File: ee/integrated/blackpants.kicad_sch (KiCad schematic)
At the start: 24 parts, among them J3 Conn_ARM_SWD_TagConnect_TC203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, SW1 SW_Push, U1 STM32F042C6Ux, U11 TPSGM7227YUWQ10G

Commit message: Added a523 components.
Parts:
- removed C10, C11, C33, C6, C8, C9: 100nF, Capacitor_SMD:C_0402_1005Metric, symbol Device:C_Small
- removed C7: 1uF, Capacitor_SMD:C_0402_1005Metric, symbol Device:C_Small
- removed D6: LED, LED_SMD:LED_0603_1608Metric, symbol Device:LED
- removed J3: Conn_ARM_SWD_TagConnect_TC2030-NL, Connector:Tag-Connect_TC2030-IDC-NL_2x03_P1.27mm_Vertical, symbol Connector:Conn_ARM_SWD_TagConnect_TC2030-NL
- removed R2, R33: 1k, Resistor_SMD:R_0402_1005Metric, symbol Device:R
- removed R26: 100K, Resistor_SMD:R_0402_1005Metric, symbol Device:R_Small
- removed SW1: SW_Push, Button_Switch_SMD:SW_Push_1P1T_NO_CK_KSC7xxJ, symbol Switch:SW_Push
- removed TP2, TP3: TestPoint, TestPoint:TestPoint_Pad_1.0x1.0mm, symbol Connector:TestPoint
- removed U1: STM32F042C6Ux, Package_DFN_QFN:QFN-48-1EP_7x7mm_P0.5mm_EP5.6x5.6mm, symbol MCU_ST_STM32F0:STM32F042C6Ux
- removed U11: TPSGM7227YUWQ10G, Package_DFN_QFN:UQFN-10_1.4x1.8mm_P0.4mm, symbol Interface_USB:FSUSB42MUX
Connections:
- no-connect marks 0 -> 1
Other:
- sheet USB renamed USB Hub
- removed sheet DSI Bridge and Backlight
- removed sheet Hardware
- removed sheet Keyboard
- added sheet 2GB LPDDR4 (a523_memory.kicad_sch)
- added sheet 5V / 3.3V peripherals (peripheral_power.kicad_sch)
- added sheet A523 SD and GPIO (a523_gpio.kicad_sch)
- added sheet A523 Standby IO (a523_always_on_io.kicad_sch)
- added sheet A523 USB PHY (a523_usb.kicad_sch)
- added sheet AXP717C + AXP323 (a523_power.kicad_sch)
- added sheet Display / backlight (dsi.kicad_sch)
- added sheet Display DSI (a523_display_io.kicad_sch)
- added sheet MicroSD boot (sdcard.kicad_sch)
- added sheet Recovery / UART / I2C (console.kicad_sch)
- added sheet STM32 + Keyboard (stm32.kicad_sch)
- added sheet SoC support (a523_soc.kicad_sch)
- added sheet Wi-Fi / Bluetooth (wifi.kicad_sch)
- added sheet Wi-Fi / Bluetooth1 (a523_wifi_io.kicad_sch)
- sheet Power & USB ports: added BAT_TS, CHGLED_N, MCU_USB_DM, MCU_USB_DP, PMIC_CC1, PMIC_CC2, PMIC_USB_DM, PMIC_USB_DP, PWRON, VBUS_PRESENT; removed USB{D+ D-}
- sheet USB Hub ports: added HUB_CONSOLE_DM, HUB_CONSOLE_DP, HUB_MCU_DM, HUB_MCU_DP, USB_HOST_DM, USB_HOST_DP; removed USB3{D+ D-}, USB_DET

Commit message: Working on the schematic.
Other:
- sheet Display DSI renamed A523 Display DSI
- sheet Wi-Fi / Bluetooth renamed RTL8723DS
- sheet Wi-Fi / Bluetooth1 renamed A523 Wifi and BT
- removed sheet AXP717C + AXP323
- removed sheet SoC support
- added sheet A523 Analog straps (a523_analog.kicad_sch)
- added sheet A523 CPU bypass (a523_cpu_bypass.kicad_sch)
- added sheet A523 Core supplies (a523_core.kicad_sch)
- added sheet A523 Ground balls (a523_ground.kicad_sch)
- added sheet AXP 323 CPU big (a523_axp323.kicad_sch)
- added sheet AXP717 Charger (a523_charger.kicad_sch)
- added sheet AXP717 LDO rails (a523_ldos.kicad_sch)
- added sheet AXP717 Main buck rails (a523_bucks.kicad_sch)
- added sheet Clocks / reset / boot (a523_system.kicad_sch)
- sheet A523 Display DSI ports: added DSI{DSI}; removed DSI_CKN, DSI_CKP, DSI_D0N, DSI_D0P, DSI_D1N, DSI_D1P
- sheet A523 SD and GPIO ports: added SD0{SD}; removed A523_I2C1_SCL, A523_I2C1_SDA, SD0_CLK, SD0_CMD, SD0_D0, SD0_D1, SD0_D2, SD0_D3, SD0_DET
- sheet A523 Standby IO ports: added PMU{I2C}; removed PMU_SCL, PMU_SDA
- sheet A523 USB PHY ports: added USB0{USB}, USB_HOST{USB}; removed USB0_DM, USB0_DP, USB_HOST_DM, USB_HOST_DP
- sheet A523 Wifi and BT ports: added BT{UART}, SD1{SD}; removed BT_CTS_N, BT_RTS_N, BT_RXD, BT_TXD, SD1_CLK, SD1_CMD, SD1_D0, SD1_D1, SD1_D2, SD1_D3
- sheet Display / backlight ports: added DSI{DSI}; removed DSI_CKN, DSI_CKP, DSI_D0N, DSI_D0P, DSI_D1N, DSI_D1P
- sheet MicroSD boot ports: added SD0{SD}; removed SD0_CLK, SD0_CMD, SD0_D0, SD0_D1, SD0_D2, SD0_D3, SD0_DET
- sheet RTL8723DS ports: added BT{UART}, SD1{SD}; removed BT_CTS_N, BT_RTS_N, BT_RXD, BT_TXD, SD1_CLK, SD1_CMD, SD1_D0, SD1_D1, SD1_D2, SD1_D3
- sheet Recovery / UART / I2C ports: added USB0{USB}; removed A523_I2C1_SCL, A523_I2C1_SDA, USB0_DM, USB0_DP
- sheet STM32 + Keyboard ports: added none; removed BL_PWM
- sheet USB Hub ports: added USB_HOST{USB}; removed USB_HOST_DM, USB_HOST_DP
- note added: "Allwinner A523"
- moved on the sheet: H1, H2, H3, H4, H6, H7

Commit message: Removed USB sheets and moved the parts to the main sheets.
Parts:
- added BT1: Protected 18650 / 1S Li-ion, BH-18650-B1BA002:BH-18650-B1BA002, symbol BH-18650-B1BA002:BH-18650-B1BA002
- added C121, C401, C901: 100nF, Capacitor_SMD:C_0402_1005Metric, symbol Device:C_Small
- added C902: 10nF, Capacitor_SMD:C_0402_1005Metric, symbol Device:C_Small
- added D902: Charge status, LED_SMD:LED_0603_1608Metric, symbol Device:LED
- added F1: 4A hold, Fuse:Fuse_1812_4532Metric, symbol Device:Polyfuse
- added J101: USB-C / recovery, Connector_USB:USB_C_Receptacle_GCT_USB4105-xx-A_16P_TopMnt_Horizontal, symbol Connector:USB_C_Receptacle_USB2.0_16P
- added J8: USB-C / charge + keyboard, Connector_USB:USB_C_Receptacle_HRO_TYPE-C-31-M-12, symbol Connector:USB_C_Receptacle_USB2.0_16P
- added PWR_BUTTON1: Power, PTS847MM160LSMTR2_LFS:SW_PTS847MM160LSMTR2_LFS, symbol PTS847MM160LSMTR2_LFS:PTS847MM160LSMTR2_LFS
- added R121, R122: 5.1k, Resistor_SMD:R_0402_1005Metric, symbol Device:R_Small
- added R123, R905: 100k, Resistor_SMD:R_0402_1005Metric, symbol Device:R_Small
- added R124, R906: 150k, Resistor_SMD:R_0402_1005Metric, symbol Device:R_Small
- added R901, R902: 1k, Resistor_SMD:R_0402_1005Metric, symbol Device:R_Small
- added R903, R904: 470, Resistor_SMD:R_0402_1005Metric, symbol Device:R_Small
- added R907: 2.2k, Resistor_SMD:R_0402_1005Metric, symbol Device:R_Small
- added SW101: FEL / recovery, Button_Switch_SMD:SW_SPST_TL3342, symbol Switch:SW_Push
- added TH901: 10k @25C / cell-attached NTC, Connector_Wire:SolderWire-0.5sqmm_1x02_P4.6mm_D0.9mm_OD2.1mm, symbol Device:Thermistor_NTC
- added U101, U12: USBLC6-2SC6, Package_TO_SOT_SMD:SOT-23-6, symbol Power_Protection:USBLC6-2SC6
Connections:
- net BAT_TS: now also C902.1, TH901.1
- net CHGLED_N: now also D902.1 (K)
- net FEL_N: now also SW101.1
- net PMIC_CC1: now also R901.2
- net PMIC_CC2: now also R902.2
- net PMIC_USB_DM: now also R904.2
- net PMIC_USB_DP: now also R903.2
- net PWRON: now also PWR_BUTTON1.1, PWR_BUTTON1.3
- net USB0_VBUS_DET: now also R123.2, R124.1
- net USB_DET: now also R905.2, R906.1
- new net: BT1.1 (+), F1.2
- new net: J8.A7 (D-), J8.B7 (D-), R904.1, U12.1 (I/O1)
- new net: J8.A6 (D+), J8.B6 (D+), R903.1, U12.3 (I/O2)
- new net: J101.A7 (D-), J101.B7 (D-), U101.1 (I/O1)
- new net: J101.A6 (D+), J101.B6 (D+), U101.3 (I/O2)
- new net: J8.A5 (CC1), R901.1
- new net: J8.B5 (CC2), R902.1
- new net: J101.A5 (CC1), R121.2
- new net: J101.B5 (CC2), R122.2
- new net: D902.2 (A), R907.2
- new net +3V3: C401.1
- new net GND: BT1.2 (-), C121.2, C401.2, C901.2, C902.2, J101.A1 (GND), J101.A12 (GND), J101.B1 (GND), J101.B12 (GND), J101.SH (SHIELD), J8.A1 (GND), J8.A12 (GND), J8.B1 (GND), J8.B12 (GND), J8.SH (SHIELD), PWR_BUTTON1.2, PWR_BUTTON1.S1 (SHIELD), PWR_BUTTON1.S2 (SHIELD), R121.1, R122.1, R124.2, R906.2, SW101.2, TH901.2, U101.2 (GND), U12.2 (GND)
- new net STM32 + Keyboard/USB3.D+: U12.4 (I/O2)
- new net STM32 + Keyboard/USB3.D-: U12.6 (I/O1)
- new net USB0.DM: U101.6 (I/O1)
- new net USB0.DP: U101.4 (I/O2)
- new net USB0_VBUS: C121.1, J101.A4 (VBUS), J101.A9 (VBUS), J101.B4 (VBUS), J101.B9 (VBUS), R123.1, U101.5 (VBUS)
- new net VBAT: F1.1
- new net VBUS: C901.1, J8.A4 (VBUS), J8.A9 (VBUS), J8.B4 (VBUS), J8.B9 (VBUS), R905.1, U12.5 (VBUS)
- new net VSYS: R907.1
- no-connect marks 1 -> 5
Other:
- sheet Clocks / reset / boot renamed A523 Clocks
- removed sheet Power & USB
- removed sheet Recovery / UART / I2C
- sheet A523 Clocks ports: added none; removed CLK32K
- sheet RTL8723DS ports: added none; removed CLK32K
- sheet USB Hub ports: added none; removed HUB_CONSOLE_DM, HUB_CONSOLE_DP
- note added: "Battery + Protection"

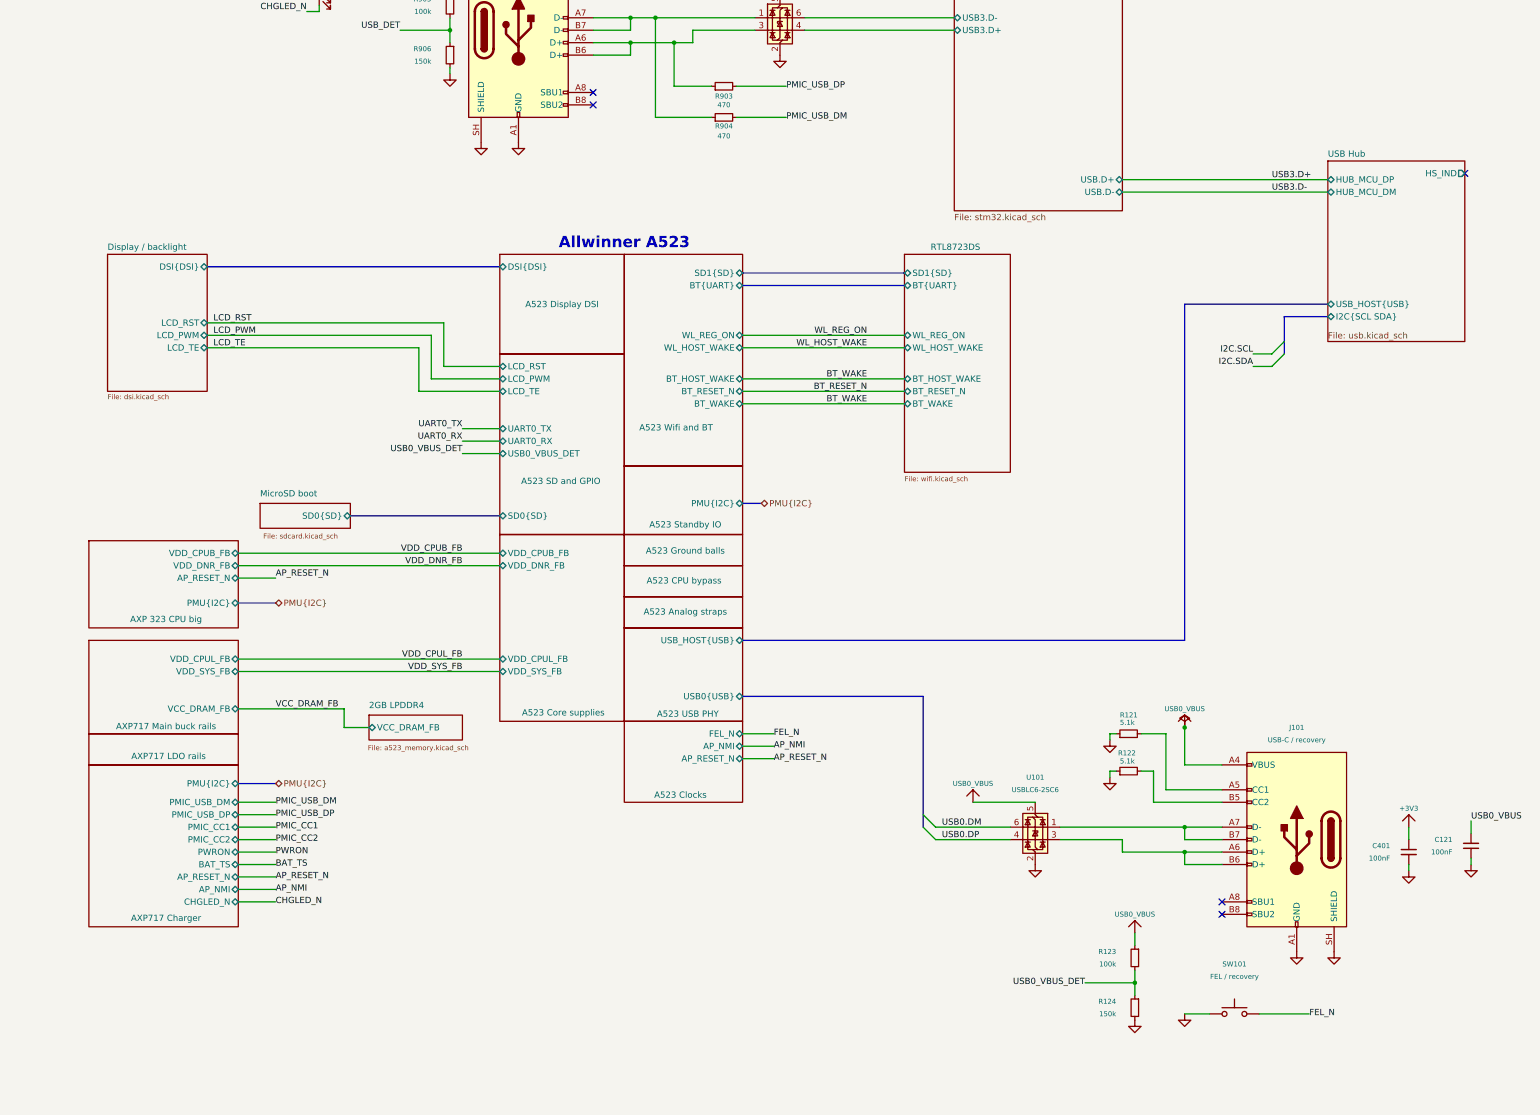
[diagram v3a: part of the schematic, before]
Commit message: Cleaned up routing.
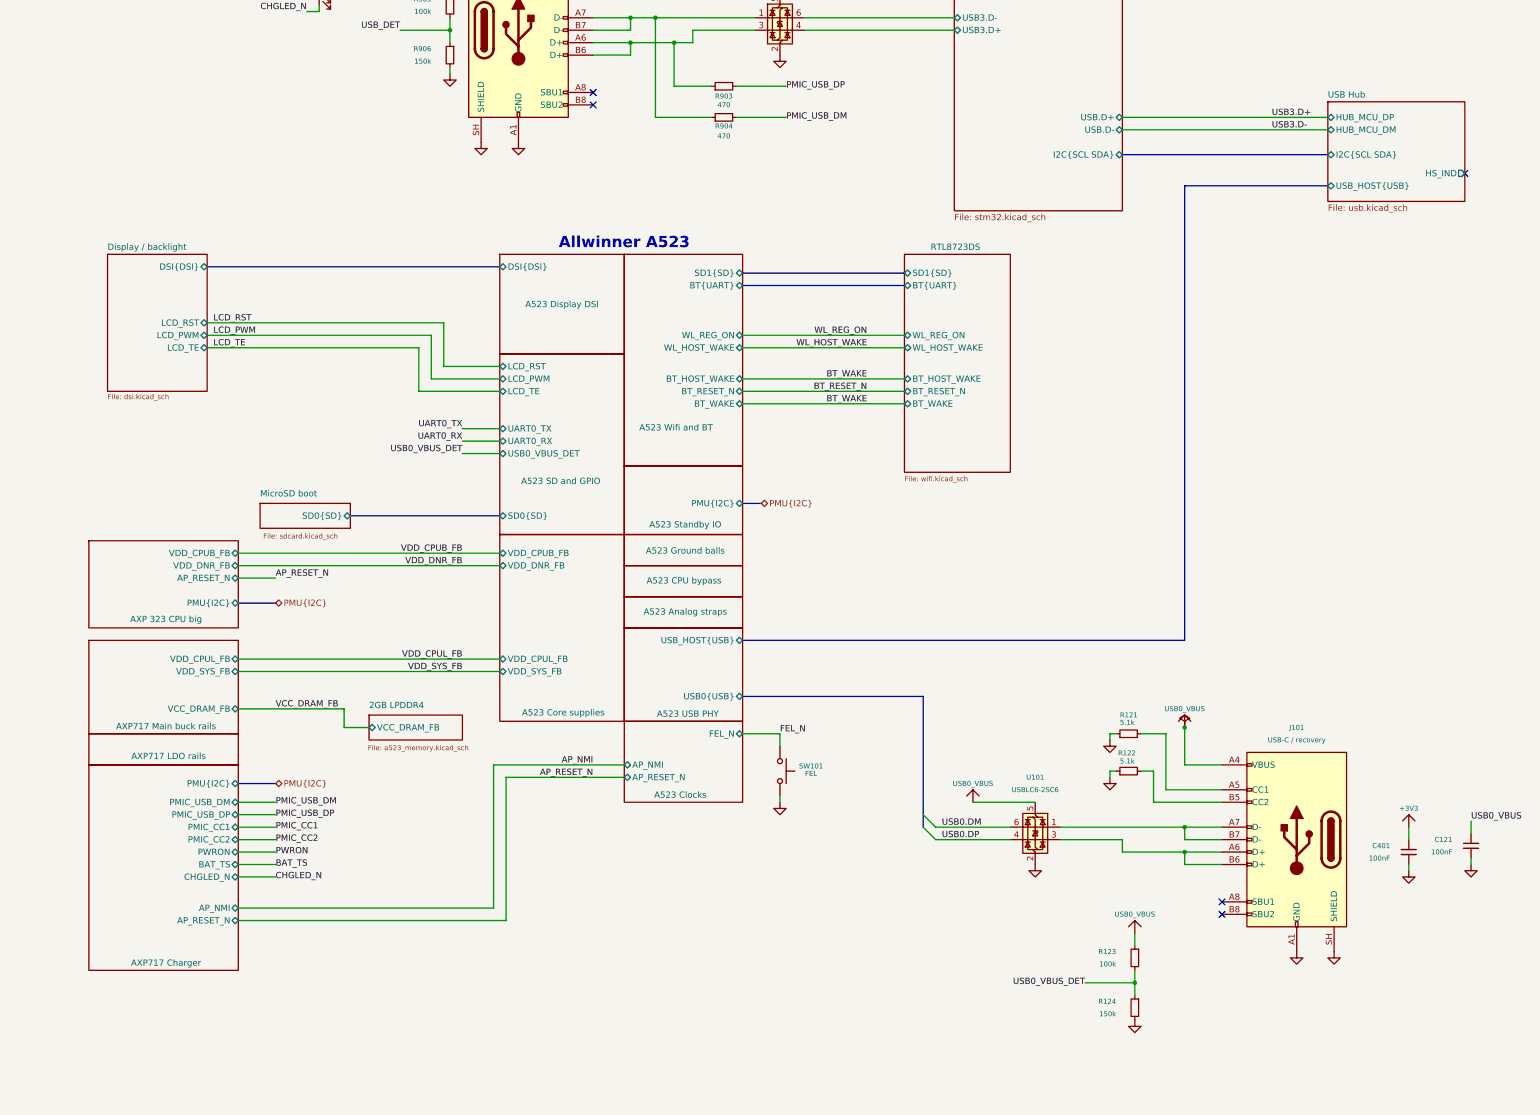
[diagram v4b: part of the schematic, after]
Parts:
- SW101: value FEL / recovery -> FEL
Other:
- sheet STM32 + Keyboard ports: added I2C{SCL SDA}; removed none
- moved on the sheet: SW101

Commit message: Worked on the layout.
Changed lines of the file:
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@@
 		)
 	)
-	(label "BT_WAKE"
+	(label "BT_HOST_WAKE"
 		(at 267.97 114.3 180)
 		(effects
